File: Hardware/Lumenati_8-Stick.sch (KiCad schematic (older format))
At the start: 20 parts, among them J1 CONN_041X04_NO_SILK, J2 CONN_041X04_NO_SILK, U1 APA102, U2 APA102, U3 APA102, U4 APA102, U5 APA102, U6 APA102, U7 APA102, U8 APA102

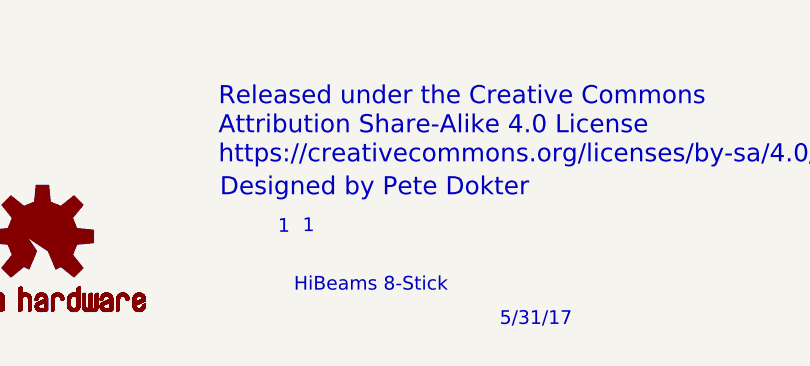
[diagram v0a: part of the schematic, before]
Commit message: Changed all the names to Lumenati.
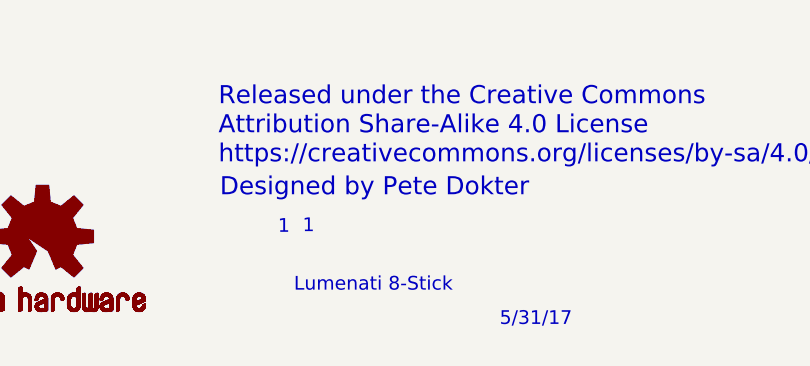
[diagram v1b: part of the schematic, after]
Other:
- note added: "Lumenati 8-Stick"
- note removed: "HiBeams 8-Stick"
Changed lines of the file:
@@
 5/31/17
 Text Notes 7350 7500 0    60   ~ 0
-HiBeams 8-Stick
+Lumenati 8-Stick
 $Comp
 L +5V #PWR07

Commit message: Updated version to v10.
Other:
- note added: "v10"
- note removed: "v01"
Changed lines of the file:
@@
 LIBS:APA102
 LIBS:apa102c
-LIBS:HiBeam_8-Stick-cache
+LIBS:Lumenati_8-Stick-cache
 EELAYER 26 0
 EELAYER END
@@
 $EndComp
 Text Notes 10600 7650 0    60   ~ 0
-v01
+v10
 Text Notes 8250 7650 0    60   ~ 0
 5/31/17
